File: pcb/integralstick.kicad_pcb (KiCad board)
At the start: 4 copper layers, 219 parts, among them J1 CONN_INTEGRALSTICK_FPGA_DEVICE, J2 CONN_INTEGRALSTICK_MCU_DEVICE, Q1 SSM6N58NU, Q2 SSM6N58NU, Q3 SSM6N58NU, U1 STM32F777NIH6‎, U10 DSC6083MI2A-032K768, U12 DSC6001HI2A-025.0000‎, U2 XC7A50T-1FTG256C, U3 S27KS0641, U4 S27KS0641, U5 KSZ9031RN, U6 S25FL064LABNFI011‎, U7 LTC3374-QFN, U8 DSC6001HI2A-025.0000, U9 AT24MAC402-UDFN

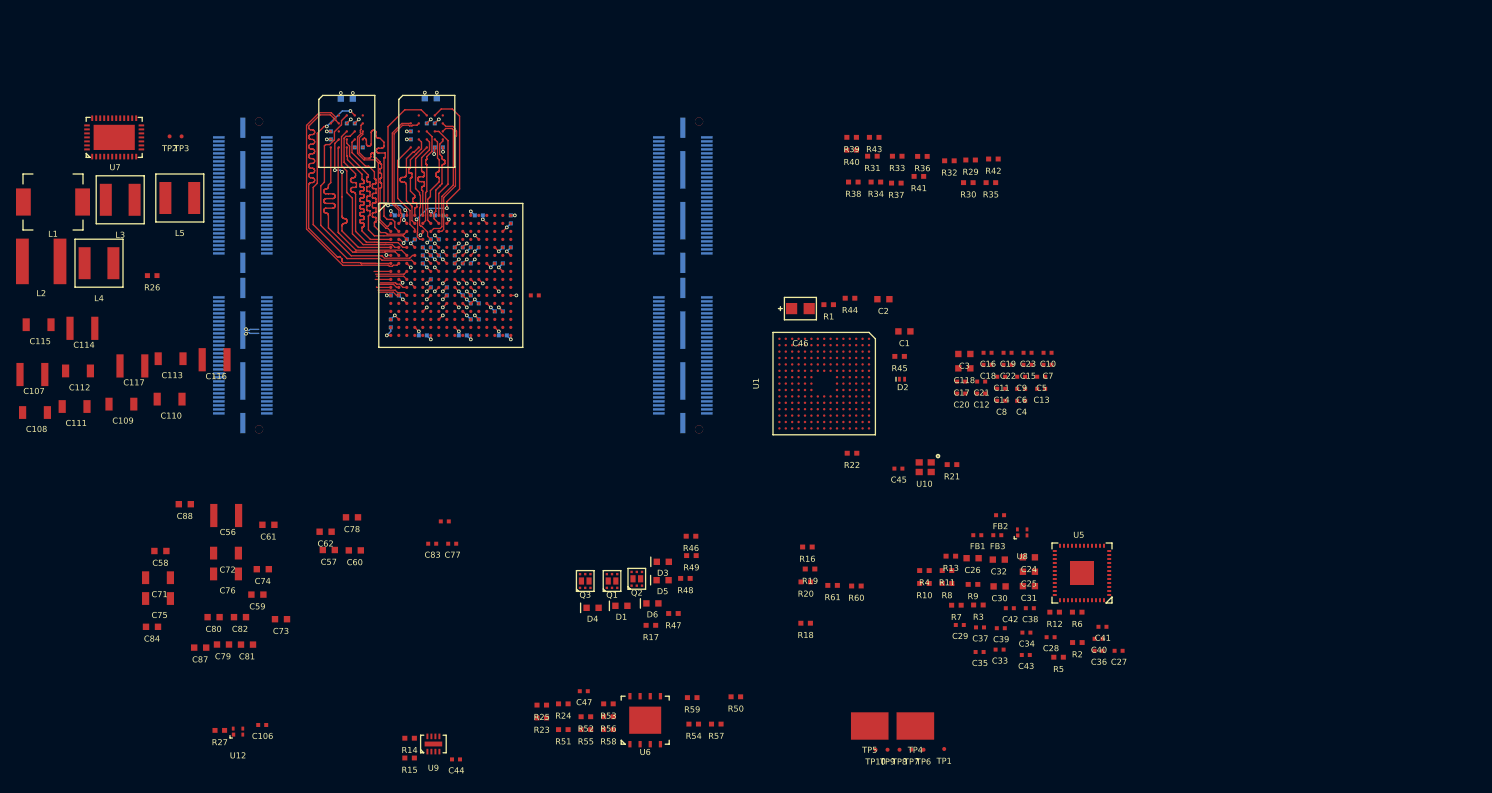
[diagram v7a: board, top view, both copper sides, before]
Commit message: Initial BGA fanout for 3.3V GPIO. Not complete.
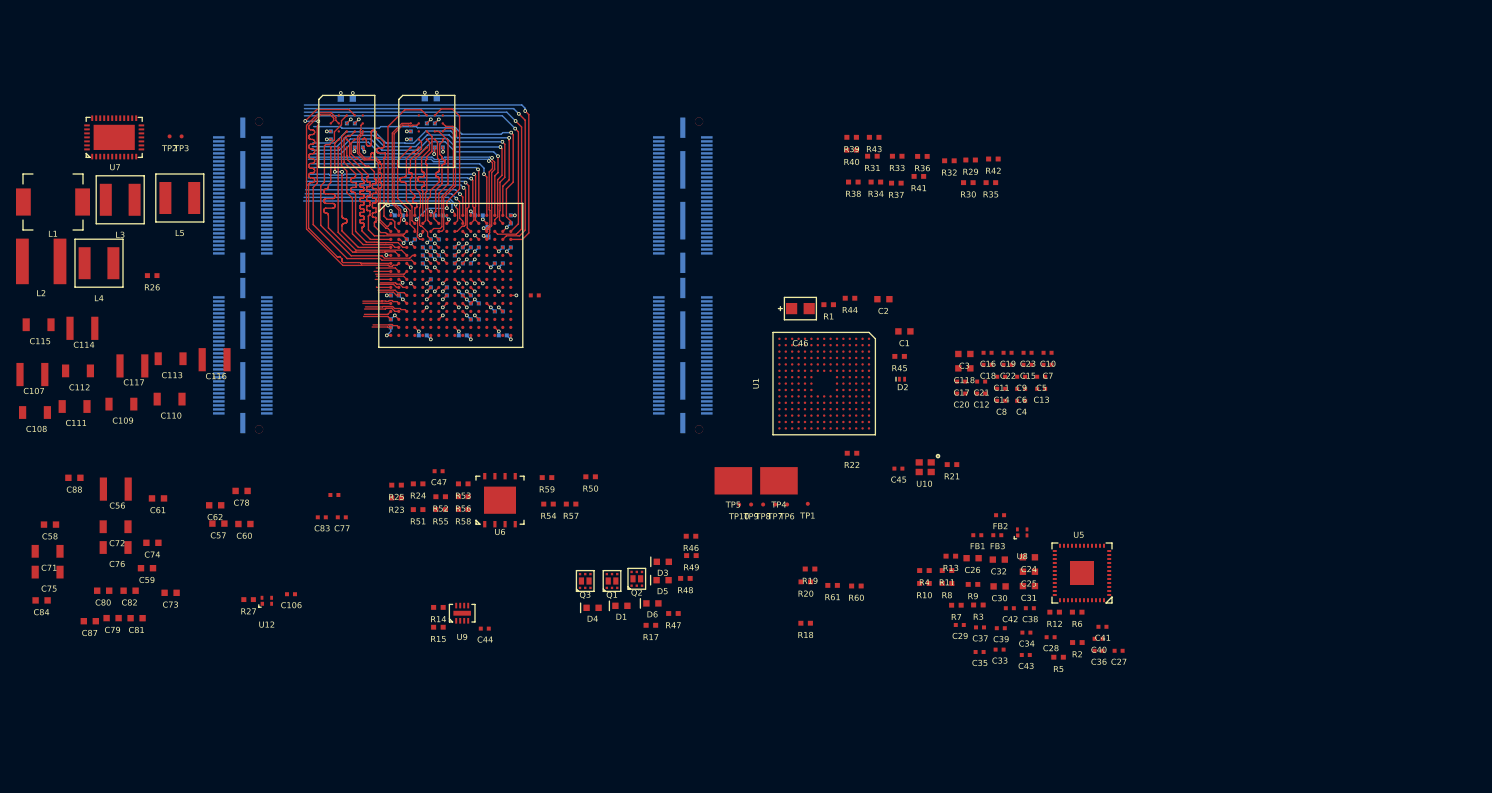
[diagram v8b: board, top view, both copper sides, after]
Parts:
- R16: moved to B.Cu
- moved R16 56.1 mm to (68.7, 37.6), turned to 90 degrees
- moved TP5 35.1 mm to (99.3, 68.7)
- moved TP1 35.1 mm to (108.6, 71.5)
- moved TP10 35.1 mm to (100.0, 71.6)
- moved TP4 35.1 mm to (105.0, 68.7)
- moved TP6 35.1 mm to (106.0, 71.6)
- moved TP7 35.1 mm to (104.5, 71.6)
- moved TP8 35.1 mm to (103.0, 71.6)
- moved TP9 35.1 mm to (101.5, 71.6)
- moved C47 32.9 mm to (62.5, 67.5)
- moved R23 32.9 mm to (57.2, 70.8)
- moved R24 32.9 mm to (59.9, 69.1)
- moved R25 32.9 mm to (57.2, 69.2)
- moved R50 32.9 mm to (81.5, 68.2)
- moved R51 32.9 mm to (59.9, 72.3)
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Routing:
- net /FPGA/IO_3V3_28: track 0.00 -> 46.1 mm, vias 0 -> 1
- net /FPGA/IO_3V3_26: track 0.00 -> 45.2 mm, vias 0 -> 1
- net /FPGA/IO_3V3_22: track 0.00 -> 44.4 mm, vias 0 -> 1
- net /FPGA/IO_3V3_18: track 0.00 -> 40.4 mm, vias 0 -> 1
- net /FPGA/IO_3V3_19: track 0.00 -> 37.4 mm, vias 0 -> 1
- net /FPGA/IO_3V3_17: track 0.00 -> 36.9 mm, vias 0 -> 1
- net /FPGA/IO_3V3_16: track 0.00 -> 36.6 mm, vias 0 -> 1
- net /FPGA/IO_3V3_15: track 0.00 -> 35.8 mm, vias 0 -> 1
- net /FPGA/IN_3V3_0_P: track 0.00 -> 35.3 mm, vias 0 -> 2
- net /FPGA/IN_3V3_0_N: track 0.00 -> 33.7 mm, vias 0 -> 2
- net /FPGA/IO_3V3_25: track 0.00 -> 33.4 mm, vias 0 -> 1
- net /FPGA/IO_3V3_14: track 0.00 -> 27.9 mm, vias 0 -> 1
- net /FPGA/IO_3V3_8: track 0.00 -> 27.2 mm, vias 0 -> 1
- net /FPGA/IO_3V3_9: track 0.00 -> 26.8 mm, vias 0 -> 1
- net /FPGA/CLK_3V3_0: track 0.00 -> 26.5 mm, vias 0 -> 1
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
